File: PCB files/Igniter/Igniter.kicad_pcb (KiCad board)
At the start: 2 copper layers, 124.9 x 69.6 mm, 56 parts, among them IC1 74HC4050, J1 PT, J10 SL3, J11 SL4, J12 SL5, J13 Micro_SD_Card, J2 PT, J3 PT, J4 PT, J5 Battery, J6 COIL, J7 COIL, J8 SL1, J9 SL2, Q1 IGN, Q2 Q_NMOS_GDSD, Q3 Q_NMOS_GDSD, Q4 Q_NMOS_GDSD, Q5 Q_NMOS_GDSD, Q6 Q_NMOS_GDSD, SW1 ARM, U2 FDS8984, U3 FDS8984, U4 FDS8984

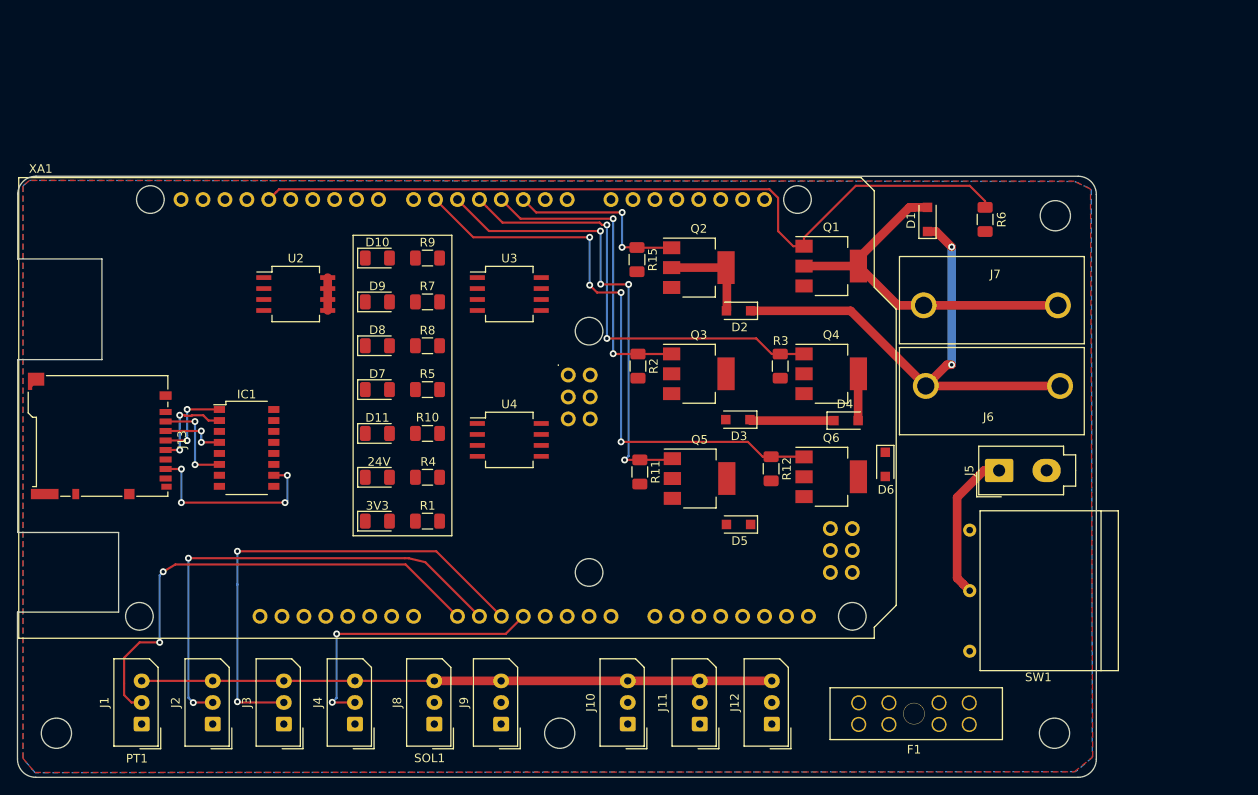
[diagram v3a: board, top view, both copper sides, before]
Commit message: 1/15/2020
-Changed schematic grid to 10 mil and moved components onto grid
-Continued board routing
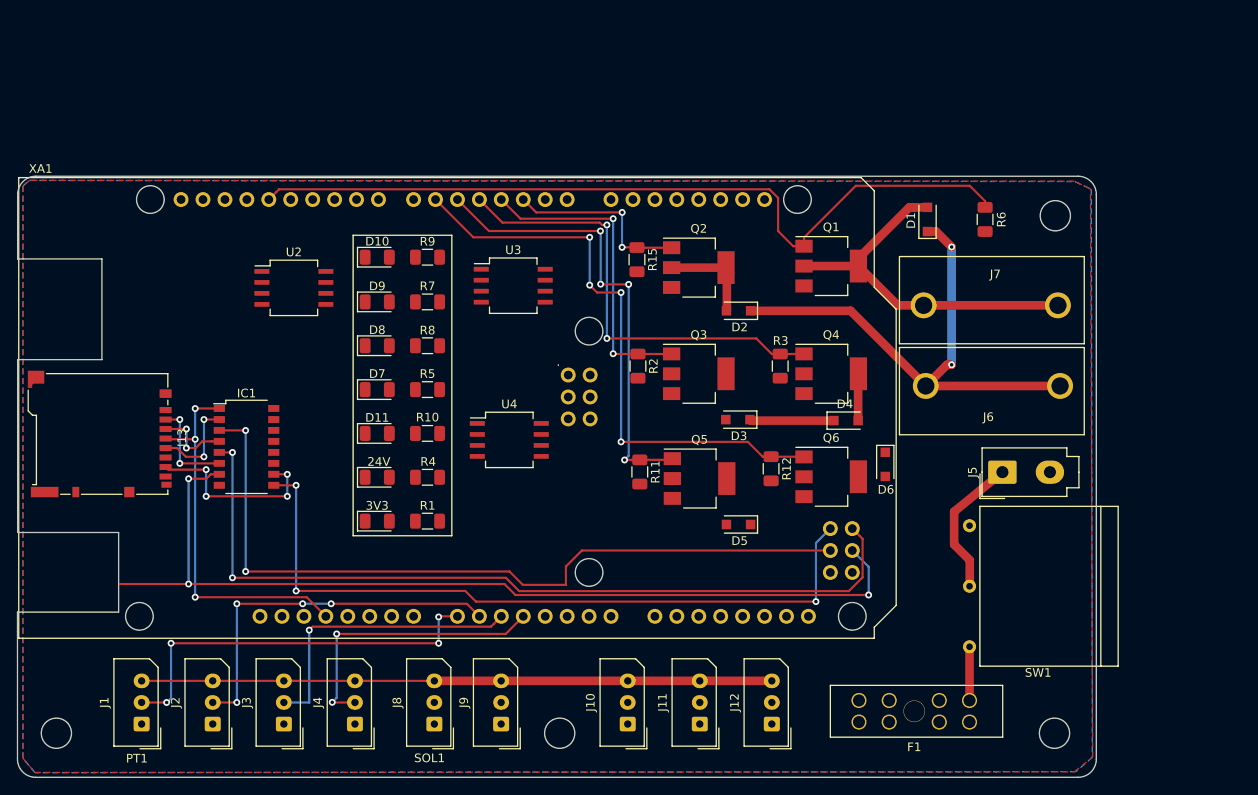
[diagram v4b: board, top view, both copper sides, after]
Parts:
- moved U3 1.07 mm to (142.5, 98.8)
- moved U2 0.74 mm to (117.1, 99.1)
- moved SW1 0.52 mm to (195.3, 133.6)
- moved J5 0.43 mm to (199.1, 120.4)
- moved F1 0.28 mm to (188.9, 148.1)
- moved J13 0.23 mm to (94.6, 116.0)
- moved IC1 0.12 mm to (111.6, 117.5)
- moved D10 0.10 mm to (126.7, 95.5)
- moved R9 0.10 mm to (132.6, 95.5)
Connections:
- IC1 pad 11: GNDREF -> (no net)
- IC1 pad 12: Net-(IC1-Pad12) -> (no net)
- IC1 pad 13: Net-(IC1-Pad13) -> (no net)
- IC1 pad 15: Net-(IC1-Pad15) -> (no net)
- IC1 pad 16: Net-(IC1-Pad16) -> (no net)
- IC1 pad 3: Net-(IC1-Pad3) -> /CLK
- IC1 pad 5: Net-(IC1-Pad5) -> /MOSI
- IC1 pad 9: Net-(IC1-Pad9) -> /MISO
- J13 pad 1: Net-(J13-Pad1) -> (no net)
- J13 pad 8: Net-(J13-Pad8) -> (no net)
- J13 pad 9: Net-(J13-Pad9) -> (no net)
- U4 pad 3: Net-(U4-Pad3) -> (no net)
- U4 pad 4: Net-(U4-Pad4) -> (no net)
- U4 pad 5: Net-(U4-Pad5) -> (no net)
- U4 pad 6: Net-(U4-Pad6) -> (no net)
- XA1 pad 5V1: Net-(XA1-Pad5V1) -> (no net)
- XA1 pad 5V2: Net-(XA1-Pad5V2) -> (no net)
- XA1 pad A10: Net-(XA1-PadA10) -> (no net)
- XA1 pad A11: Net-(XA1-PadA11) -> (no net)
- XA1 pad A12: Net-(XA1-PadA12) -> (no net)
- XA1 pad A13: Net-(XA1-PadA13) -> (no net)
- XA1 pad A14: Net-(XA1-PadA14) -> (no net)
- XA1 pad A15: Net-(XA1-PadA15) -> (no net)
- XA1 pad A4: Net-(XA1-PadA4) -> (no net)
- XA1 pad A5: Net-(XA1-PadA5) -> (no net)
- XA1 pad A6: Net-(XA1-PadA6) -> (no net)
- XA1 pad A7: Net-(XA1-PadA7) -> (no net)
- XA1 pad A8: Net-(XA1-PadA8) -> (no net)
- XA1 pad A9: Net-(XA1-PadA9) -> (no net)
- XA1 pad AREF: Net-(XA1-PadAREF) -> (no net)
- XA1 pad D0: Net-(XA1-PadD0) -> (no net)
- XA1 pad D1: Net-(XA1-PadD1) -> (no net)
- XA1 pad D10: Net-(XA1-PadD10) -> (no net)
- XA1 pad D11: Net-(XA1-PadD11) -> (no net)
- XA1 pad D12: Net-(XA1-PadD12) -> (no net)
- XA1 pad D14: Net-(XA1-PadD14) -> (no net)
- XA1 pad D15: Net-(XA1-PadD15) -> (no net)
- XA1 pad D16: Net-(XA1-PadD16) -> (no net)
- XA1 pad D17: Net-(XA1-PadD17) -> (no net)
- XA1 pad D18: Net-(XA1-PadD18) -> (no net)
- XA1 pad D19: Net-(XA1-PadD19) -> (no net)
- XA1 pad D20: Net-(XA1-PadD20) -> (no net)
- XA1 pad D21: Net-(XA1-PadD21) -> (no net)
- XA1 pad D50: Net-(XA1-PadD50) -> /MISO
- XA1 pad D51: Net-(XA1-PadD51) -> /MOSI
- XA1 pad D52: Net-(XA1-PadD52) -> /CLK
- XA1 pad D7: Net-(XA1-PadD7) -> (no net)
- XA1 pad D8: Net-(XA1-PadD8) -> (no net)
- XA1 pad D9: Net-(XA1-PadD9) -> (no net)
- XA1 pad IORF: Net-(XA1-PadIORF) -> (no net)
- XA1 pad MISO: Net-(IC1-Pad9) -> (no net)
- XA1 pad MOSI: Net-(IC1-Pad5) -> (no net)
- XA1 pad RST1: Net-(XA1-PadRST1) -> (no net)
- XA1 pad RST2: Net-(XA1-PadRST2) -> (no net)
- XA1 pad SCK: Net-(IC1-Pad3) -> (no net)
- XA1 pad SCL: Net-(XA1-PadSCL) -> (no net)
- XA1 pad SDA: Net-(XA1-PadSDA) -> (no net)
- XA1 pad VIN: Net-(XA1-PadVIN) -> (no net)
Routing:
- net /CS: track 0.00 -> 109.2 mm, vias 0 -> 3
- net /MOSI: track 0.00 -> 96.4 mm, vias 0 -> 2
- net /CLK: track 0.00 -> 90.6 mm, vias 0 -> 2
- net /MISO: track 0.00 -> 84.7 mm, vias 0 -> 3
- net +3V3: track 9.84 -> 44.2 mm, vias 2 -> 3
- net /PT2: track 56.5 -> 34.2 mm, vias 2 -> 1
- net /PT1: track 55.6 -> 42.9 mm, vias 2 -> 4
- net /PT0: track 56.7 -> 46.2 mm, vias 2 -> 4
- net Net-(F1-Pad5): track 0.00 -> 6.22 mm
- net +24V: track 147.2 -> 143.4 mm
- net Net-(IC1-Pad4): track 7.54 -> 8.75 mm
- net Net-(IC1-Pad10): track 22.6 -> 21.4 mm
- net Net-(J5-Pad1): track 17.6 -> 16.6 mm

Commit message: 1/16/2020
-Continued board routing
-Rearranged board LEDs and added labels
-Removed hierarchical sheet, combined schematic into one sheet
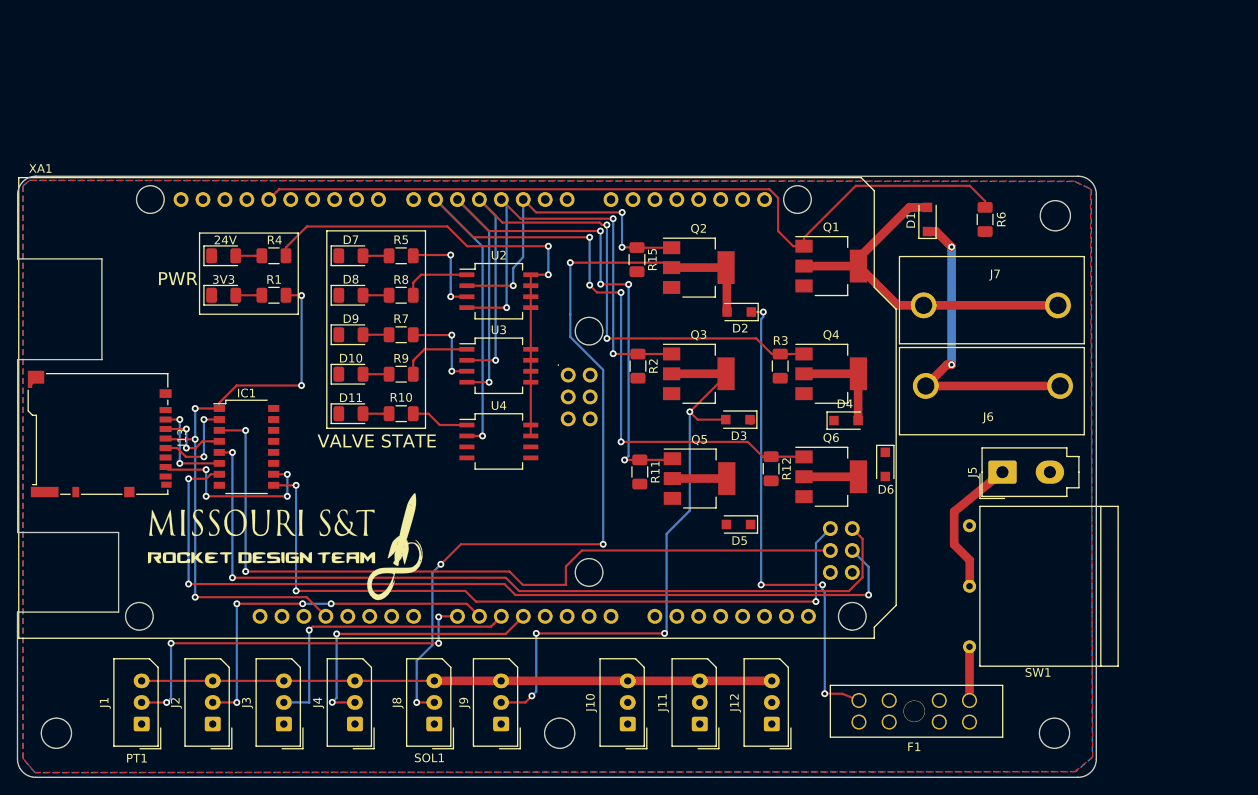
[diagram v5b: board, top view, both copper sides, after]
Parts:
- added G***: LOGO, Board images:RocketLogo, F.Cu at (116.2, 129.2)
- moved R1 31.6 mm to (114.8, 99.9)
- moved D12 31.6 mm to (109.0, 99.9)
- moved R4 31.2 mm to (114.8, 95.3)
- moved D13 31.2 mm to (109.0, 95.3)
- moved U2 23.7 mm to (140.8, 99.4)
- moved D7 15.8 mm to (123.7, 95.3)
- moved R5 15.8 mm to (129.5, 95.3)
- moved D10 13.9 mm to (123.7, 109.1)
- moved R9 13.9 mm to (129.5, 109.1)
- moved U3 9.42 mm to (140.8, 108.1)
- moved D8 6.59 mm to (123.7, 99.9)
- moved R8 6.59 mm to (129.5, 99.9)
- moved D9 4.87 mm to (123.7, 104.5)
- moved R7 4.87 mm to (129.5, 104.5)
- moved D11 3.81 mm to (123.7, 113.6)
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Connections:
- net Net-(Q1-Pad1) renamed /SPRK
- IC1 pad 11: (no net) -> Net-(IC1-Pad11)
- IC1 pad 12: (no net) -> Net-(IC1-Pad12)
- IC1 pad 13: (no net) -> Net-(IC1-Pad13)
- IC1 pad 15: (no net) -> Net-(IC1-Pad15)
- IC1 pad 16: (no net) -> Net-(IC1-Pad16)
- J13 pad 1: (no net) -> Net-(J13-Pad1)
- J13 pad 8: (no net) -> Net-(J13-Pad8)
- J13 pad 9: (no net) -> Net-(J13-Pad9)
- U4 pad 3: (no net) -> Net-(U4-Pad3)
- U4 pad 4: (no net) -> Net-(U4-Pad4)
- U4 pad 5: (no net) -> Net-(U4-Pad5)
- U4 pad 6: (no net) -> Net-(U4-Pad6)
- XA1 pad 5V1: (no net) -> Net-(XA1-Pad5V1)
- XA1 pad 5V2: (no net) -> Net-(XA1-Pad5V2)
- XA1 pad A10: (no net) -> Net-(XA1-PadA10)
- XA1 pad A11: (no net) -> Net-(XA1-PadA11)
- XA1 pad A12: (no net) -> Net-(XA1-PadA12)
- XA1 pad A13: (no net) -> Net-(XA1-PadA13)
- XA1 pad A14: (no net) -> Net-(XA1-PadA14)
- XA1 pad A15: (no net) -> Net-(XA1-PadA15)
- XA1 pad A4: (no net) -> Net-(XA1-PadA4)
- XA1 pad A5: (no net) -> Net-(XA1-PadA5)
- XA1 pad A6: (no net) -> Net-(XA1-PadA6)
- XA1 pad A7: (no net) -> Net-(XA1-PadA7)
- XA1 pad A8: (no net) -> Net-(XA1-PadA8)
- XA1 pad A9: (no net) -> Net-(XA1-PadA9)
- XA1 pad AREF: (no net) -> Net-(XA1-PadAREF)
- XA1 pad D0: (no net) -> Net-(XA1-PadD0)
- XA1 pad D1: (no net) -> Net-(XA1-PadD1)
- XA1 pad D10: (no net) -> Net-(XA1-PadD10)
- XA1 pad D11: (no net) -> Net-(XA1-PadD11)
- XA1 pad D12: (no net) -> Net-(XA1-PadD12)
- XA1 pad D14: (no net) -> Net-(XA1-PadD14)
- XA1 pad D15: (no net) -> Net-(XA1-PadD15)
- XA1 pad D16: (no net) -> Net-(XA1-PadD16)
- XA1 pad D17: (no net) -> Net-(XA1-PadD17)
- XA1 pad D18: (no net) -> Net-(XA1-PadD18)
- XA1 pad D19: (no net) -> Net-(XA1-PadD19)
- XA1 pad D2: SOL1 -> /SOL1
- XA1 pad D20: (no net) -> Net-(XA1-PadD20)
- XA1 pad D21: (no net) -> Net-(XA1-PadD21)
- XA1 pad D3: SOL2 -> /SOL2
- XA1 pad D4: SOL3 -> /SOL3
- XA1 pad D5: SOL4 -> /SOL4
- XA1 pad D6: SOL5 -> /SOL5
- XA1 pad D7: (no net) -> Net-(XA1-PadD7)
- XA1 pad D8: (no net) -> Net-(XA1-PadD8)
- XA1 pad D9: (no net) -> Net-(XA1-PadD9)
- XA1 pad GND2: GNDREF -> Net-(XA1-PadGND2)
- XA1 pad GND3: GNDREF -> Net-(XA1-PadGND3)
- XA1 pad GND5: GNDREF -> Net-(XA1-PadGND5)
- XA1 pad GND6: GNDREF -> Net-(XA1-PadGND5)
- XA1 pad IORF: (no net) -> Net-(XA1-PadIORF)
- XA1 pad MISO: (no net) -> Net-(XA1-PadMISO)
- XA1 pad MOSI: (no net) -> Net-(XA1-PadMOSI)
- XA1 pad RST1: (no net) -> Net-(XA1-PadRST1)
- XA1 pad RST2: (no net) -> Net-(XA1-PadRST2)
- XA1 pad SCK: (no net) -> Net-(XA1-PadSCK)
- XA1 pad SCL: (no net) -> Net-(XA1-PadSCL)
- XA1 pad SDA: (no net) -> Net-(XA1-PadSDA)
- XA1 pad VIN: (no net) -> Net-(XA1-PadVIN)
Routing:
- net Net-(D2-Pad2): track 11.3 -> 96.7 mm, vias 0 -> 4
- net +24V: track 143.4 -> 224.1 mm, vias 2 -> 8
- net Net-(D3-Pad2): track 0.00 -> 70.0 mm, vias 0 -> 4
- net SOL5: track 68.4 -> 99.8 mm, vias 4 -> 5
- net SOL4: track 53.6 -> 78.9 mm, vias 4 -> 5
- net +3V3: track 44.2 -> 67.4 mm, vias 3 -> 5
- net SOL3: track 52.8 -> 75.5 mm, vias 2 -> 3
- net SOL2: track 36.3 -> 53.7 mm, vias 2 -> 3
- net SOL1: track 21.9 -> 37.6 mm, vias 2 -> 3
- net Net-(R5-Pad2): track 0.00 -> 11.1 mm, vias 0 -> 2
- net Net-(R7-Pad2): track 0.00 -> 10.4 mm, vias 0 -> 2
- net Net-(R9-Pad1): track 0.00 -> 8.34 mm
- net Net-(R8-Pad1): track 0.00 -> 8.05 mm
- net /CS: track 109.2 -> 101.2 mm
- net Net-(R10-Pad1): track 0.00 -> 6.75 mm
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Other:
- board text added: "PWR"
- board text added: "VALVE STATE"

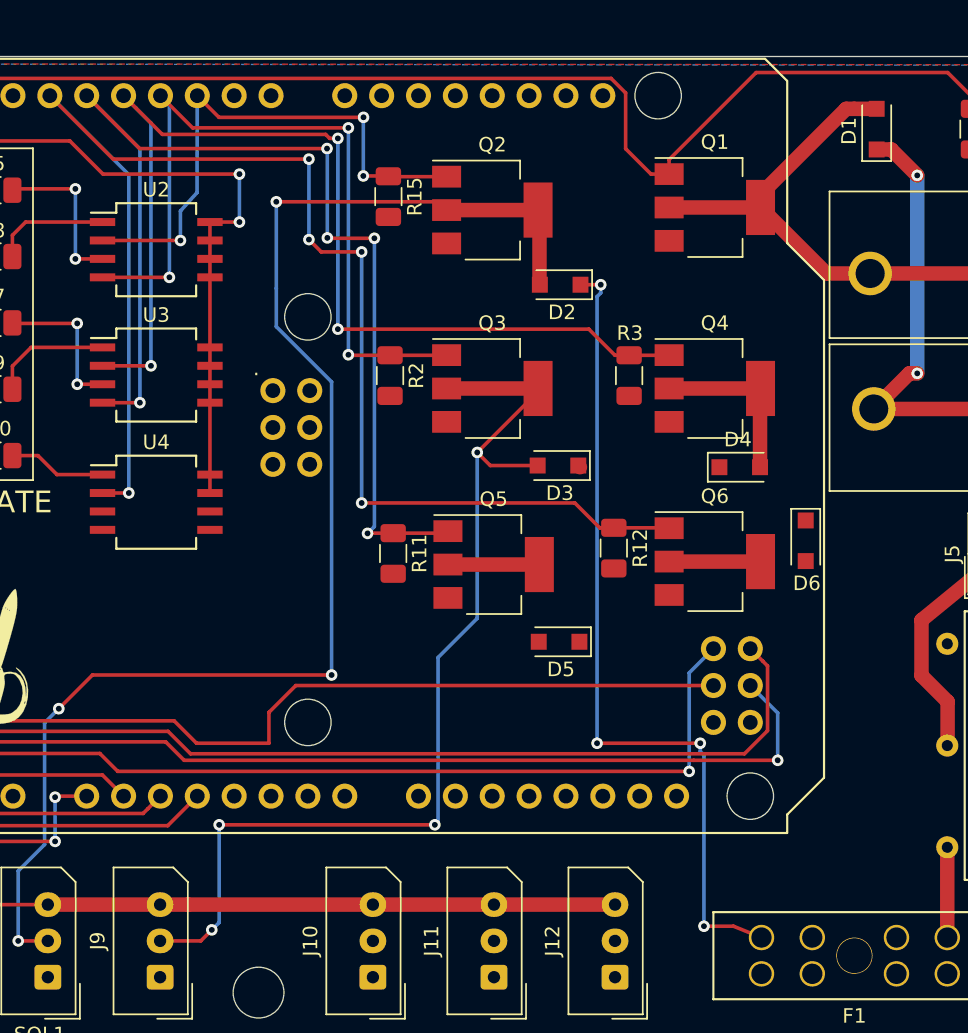
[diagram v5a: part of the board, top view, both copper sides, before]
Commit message: 1/17/2020
-Completed board routing
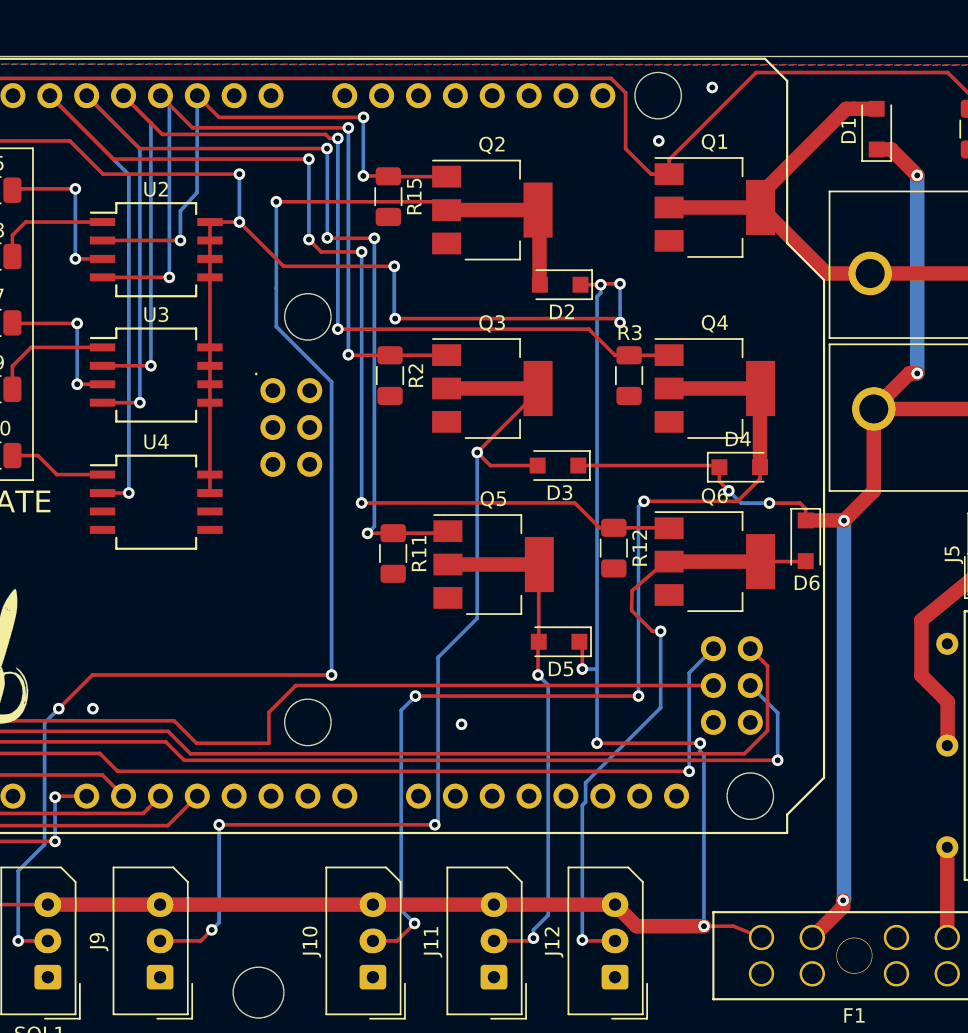
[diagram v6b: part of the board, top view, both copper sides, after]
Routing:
- net +24V: track 224.1 -> 328.0 mm, vias 8 -> 17
- net Net-(D4-Pad2): track 11.7 -> 69.9 mm, vias 0 -> 4
- net Net-(D6-Pad2): track 6.30 -> 42.5 mm, vias 0 -> 2
- net Net-(D5-Pad2): track 6.30 -> 35.6 mm, vias 0 -> 2
- net GNDREF: vias 0 -> 4
